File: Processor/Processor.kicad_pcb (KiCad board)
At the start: 2 copper layers, 100 x 100 mm, 43 parts, among them J1 Buss, J2 L2|L3, U1 MC6800, U10 74LS573, U11 74LS573, U2 74LS74, U3 74LS00, U4 74LS245, U5 74LS573, U6 74LS138, U7 GAL20V8, U8 74LS04, U9 74LS573, Y1 2.0MHz

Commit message: churn
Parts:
- added J3: L3, Connector_PinHeader_2.54mm:PinHeader_1x10_P2.54mm_Horizontal, F.Cu at (32.6, 35.2)
- J2: value L2|L3 -> L2; footprint Connector_PinSocket_2.54mm:PinSocket_2x08_P2.54mm_Horizontal -> Connector_PinHeader_2.54mm:PinHeader_1x10_P2.54mm_Horizontal
- moved C11 35.4 mm to (28.8, 42.7)
- moved U11 35.4 mm to (32.6, 47.8)
- moved RN3 20.3 mm to (96.1, 107.5), turned to 180 degrees
- moved J2 16.7 mm to (66.9, 35.2), turned to 90 degrees
- moved C9 3.85 mm to (93.6, 55.5)
- moved U9 3.85 mm to (97.2, 60.6)
- moved C10 3.81 mm to (93.6, 42.8)
- moved C3 3.81 mm to (28.8, 80.9)
- moved C8 3.81 mm to (28.8, 55.5)
- moved RN2 3.81 mm to (55.5, 107.5)
- moved U10 3.81 mm to (97.4, 47.9)
- moved U2 3.81 mm to (32.6, 73.3)
- moved U8 3.81 mm to (32.6, 60.6)
- moved U3 3.81 mm to (32.6, 86.0)
- moved C2 3.77 mm to (28.8, 68.2)
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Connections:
- J2 pad 1: Net-(J2-Pin_1) -> +5V
- J2 pad 10: Net-(J2-Pin_10) -> GND
- RN3 pad 2: A15 -> A8
- RN3 pad 3: A14 -> A9
- RN3 pad 4: A13 -> A10
- RN3 pad 5: A12 -> A11
- RN3 pad 6: A11 -> A12
- RN3 pad 7: A10 -> A13
- RN3 pad 8: A9 -> A14
- RN3 pad 9: A8 -> A15
- U11 pad 12: Net-(J2-Pin_16) -> Net-(J3-Pin_9)
- U11 pad 13: Net-(J2-Pin_14) -> Net-(J3-Pin_8)
- U11 pad 14: Net-(J2-Pin_12) -> Net-(J3-Pin_7)
- U11 pad 15: Net-(J2-Pin_10) -> Net-(J3-Pin_6)
- U11 pad 16: Net-(J2-Pin_8) -> Net-(J3-Pin_5)
- U11 pad 17: Net-(J2-Pin_6) -> Net-(J3-Pin_4)
- U11 pad 18: Net-(J2-Pin_4) -> Net-(J3-Pin_3)
- U11 pad 19: Net-(J2-Pin_2) -> Net-(J3-Pin_2)
- U5 pad 12: Net-(J2-Pin_15) -> Net-(J2-Pin_9)
- U5 pad 13: Net-(J2-Pin_13) -> Net-(J2-Pin_8)
- U5 pad 14: Net-(J2-Pin_11) -> Net-(J2-Pin_7)
- U5 pad 15: Net-(J2-Pin_9) -> Net-(J2-Pin_6)
- U5 pad 16: Net-(J2-Pin_7) -> Net-(J2-Pin_5)
- U5 pad 17: Net-(J2-Pin_5) -> Net-(J2-Pin_4)
- U5 pad 19: Net-(J2-Pin_1) -> Net-(J2-Pin_2)

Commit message: a bunch of stuff
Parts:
- removed C10, C11, C5, C9: 100n, Capacitor_THT:C_Disc_D3.0mm_W1.6mm_P2.50mm
- removed D1: S0, LED_THT:LED_Rectangular_W5.0mm_H2.0mm
- removed D2: S1, LED_THT:LED_Rectangular_W5.0mm_H2.0mm
- removed D3: S2, LED_THT:LED_Rectangular_W5.0mm_H2.0mm
- removed D4: S3, LED_THT:LED_Rectangular_W5.0mm_H2.0mm
- removed D5: S4, LED_THT:LED_Rectangular_W5.0mm_H2.0mm
- removed D6: S5, LED_THT:LED_Rectangular_W5.0mm_H2.0mm
- removed D7: S6, LED_THT:LED_Rectangular_W5.0mm_H2.0mm
- removed D8: S7, LED_THT:LED_Rectangular_W5.0mm_H2.0mm
- removed J2: L2, Connector_PinHeader_2.54mm:PinHeader_1x10_P2.54mm_Horizontal
- removed J3: L3, Connector_PinHeader_2.54mm:PinHeader_1x10_P2.54mm_Horizontal
- removed RN5: 220Ω, Resistor_THT:R_Array_SIP9
- removed U10, U11, U5, U9: 74LS573, Package_DIP:DIP-20_W7.62mm
- removed U6: 74LS138, Package_DIP:DIP-16_W7.62mm
- added G1: Logo, 0-Footprints:Crank, F.Cu at (32.7, 114.0)
- U7: value GAL20V8 -> GAL22V10
- moved C2 85.3 mm to (113.3, 79.4), turned to 180 degrees
- moved U2 76.2 mm to (108.3, 82.4), turned to 0 degrees
- moved C8 72.1 mm to (96.8, 79.4), turned to 180 degrees
- moved U8 63.1 mm to (91.8, 82.4), turned to 0 degrees
- moved Y1 57.2 mm to (113.9, 63.6), turned to 180 degrees
- moved C3 51.5 mm to (80.3, 79.4), turned to 180 degrees
- moved U3 42.8 mm to (75.3, 82.4), turned to 0 degrees
- moved R6 35.2 mm to (53.4, 61.6)
- moved C1 35.2 mm to (68.7, 56.5)
- moved R7 35.2 mm to (58.5, 61.6)
- moved R8 35.2 mm to (63.6, 61.6)
- moved U1 35.2 mm to (50.9, 54.0)
- moved U7 33.2 mm to (60.0, 69.7), turned to 0 degrees
- moved C7 30.9 mm to (65.1, 66.7), turned to 180 degrees
- moved C4 29.5 mm to (45.3, 71.7), turned to 180 degrees
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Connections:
- J1 pad 10: BANK_0 -> unconnected-(J1-Pad10)
- J1 pad 12: BANK_1 -> unconnected-(J1-Pad12)
- J1 pad 14: BANK_2 -> unconnected-(J1-Pad14)
- J1 pad 16: BANK_3 -> unconnected-(J1-Pad16)
- J1 pad 18: BANK_4 -> unconnected-(J1-Pad18)
- J1 pad 20: BANK_5 -> unconnected-(J1-Pad20)
- J1 pad 22: BANK_6 -> unconnected-(J1-Pad22)
- J1 pad 24: BANK_7 -> unconnected-(J1-Pad24)
- J1 pad 44: Φ2 -> unconnected-(J1-Pad44)
- J1 pad B3: unconnected-(J1-PadB3) -> Φ2
- U3 pad 10: Net-(U6-O1) -> GND
- U3 pad 11: LOAD_0 -> unconnected-(U3-Pad11)
- U3 pad 12: Net-(U6-O0) -> GND
- U3 pad 13: Net-(U6-O0) -> GND
- U3 pad 8: LOAD_1 -> unconnected-(U3-Pad8)
- U3 pad 9: Net-(U6-O1) -> GND
- U7 pad 10: A12 -> A8
- U7 pad 11: A11 -> GND
- U7 pad 13: A10 -> GND
- U7 pad 14: A9 -> GND
- U7 pad 17: ~{LATCH_SEL} -> GND
- U7 pad 18: BUS_OK -> GND
- U7 pad 19: ~{IO_SEL} -> BUS_OK
- U7 pad 20: ~{BANK_SEL} -> ~{IO_SEL}
- U7 pad 21: ~{ROM_SEL} -> ~{BANK_SEL}
- U7 pad 22: ~{RAM_SEL} -> ~{ROM_SEL}
- U7 pad 23: A8 -> ~{RAM_SEL}
- U7 pad 3: GND -> A15
- U7 pad 4: GND -> A14
- U7 pad 5: GND -> A13
- U7 pad 6: GND -> A12
- U7 pad 7: A15 -> A11
- U7 pad 8: A14 -> A10
- U7 pad 9: A13 -> A9
- U8 pad 10: LOAD_2 -> unconnected-(U8-Pad10)
- U8 pad 11: Net-(U6-O2) -> GND
- U8 pad 12: LOAD_3 -> unconnected-(U8-Pad12)
- U8 pad 13: Net-(U6-O3) -> GND

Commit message: ordered v01 of the cpu
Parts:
- removed C6, C7, C8: 100n, Capacitor_THT:C_Disc_D3.0mm_W1.6mm_P2.50mm
- removed the R6 at (53.4, 61.6)
- removed U3: 74LS00, Package_DIP:DIP-14_W7.62mm
- removed U8: 74LS04, Package_DIP:DIP-14_W7.62mm
- added C5: 100n, 0-Footprints:C_Disc_D5.0mm_W2.5mm_P5.00mm, F.Cu at (66.1, 55.5)
- added G2: Crankery, 0-Footprints:crankery_small, F.Cu at (112.7, 110.8)
- added G3: Motorola, 0-Footprints:Motorola, B.Cu at (69.3, 31.0)
- added G4: Crank, 0-Footprints:Crank, B.Cu at (103.4, 31.1)
- added R1: 10K, 0-Footprints:R_Axial_DIN0204_L3.6mm_D1.6mm_P7.62mm_Horizontal, F.Cu at (42.0, 66.9)
- added R2: 10K, 0-Footprints:R_Axial_DIN0204_L3.6mm_D1.6mm_P7.62mm_Horizontal, F.Cu at (92.8, 83.4)
- added R3: 10K, 0-Footprints:R_Axial_DIN0204_L3.6mm_D1.6mm_P7.62mm_Horizontal, F.Cu at (41.5, 107.5)
- added R4: 10K, 0-Footprints:R_Axial_DIN0204_L3.6mm_D1.6mm_P7.62mm_Horizontal, F.Cu at (58.5, 74.5)
- added R9: 10K, 0-Footprints:R_Axial_DIN0204_L3.6mm_D1.6mm_P7.62mm_Horizontal, F.Cu at (54.2, 107.5)
- added RN5: 4.7K, 0-Footprints:R_Array_SIP5, F.Cu at (62.3, 83.4)
- added RN6: 4.7K, 0-Footprints:R_Array_SIP5, F.Cu at (89.0, 93.6)
- added RN7: 4.7K, 0-Footprints:R_Array_SIP5, F.Cu at (66.1, 73.3)
- added RN8: 4.7K, 0-Footprints:R_Array_SIP5, F.Cu at (89.0, 58.0)
- C1: value 100n -> 100nF; footprint Capacitor_THT:C_Disc_D3.0mm_W1.6mm_P2.50mm -> 0-Footprints:C_Disc_D5.0mm_W2.5mm_P5.00mm
- C2, C3, C4: footprint Capacitor_THT:C_Disc_D3.0mm_W1.6mm_P2.50mm -> 0-Footprints:C_Disc_D5.0mm_W2.5mm_P5.00mm
- G1: value Logo -> Crank
- R5, R7, R8: footprint Resistor_THT:R_Axial_DIN0204_L3.6mm_D1.6mm_P5.08mm_Horizontal -> 0-Footprints:R_Axial_DIN0204_L3.6mm_D1.6mm_P7.62mm_Horizontal
- R6: renamed from R9; footprint Resistor_THT:R_Axial_DIN0204_L3.6mm_D1.6mm_P5.08mm_Horizontal -> 0-Footprints:R_Axial_DIN0204_L3.6mm_D1.6mm_P7.62mm_Horizontal
- RN1, RN2, RN3, RN4: footprint Resistor_THT:R_Array_SIP9 -> 0-Footprints:R_Array_SIP5
- U1: value MC6800 -> M6800; footprint Package_DIP:DIP-40_W15.24mm -> 0-Footprints:DIP-40_W15.24mm
- U2: value 74LS74 -> MC6875; footprint Package_DIP:DIP-14_W7.62mm -> 0-Footprints:DIP-16_W7.62mm
- U4: footprint Package_DIP:DIP-20_W7.62mm -> 0-Footprints:DIP-20_W7.62mm
- U7: footprint Package_DIP:DIP-24_W7.62mm -> 0-Footprints:DIP-24_W7.62mm
- Y1: value 2.0MHz -> 4.000MHz; footprint Oscillator:Oscillator_DIP-14 -> 0-Footprints:Oscillator_DIP-14
- moved G1 82.9 mm to (35.6, 31.2)
- moved R6 72.4 mm to (46.6, 107.5), turned to -90 degrees
- moved U2 65.2 mm to (54.7, 45.3)
- moved RN2 64.3 mm to (92.8, 68.2)
- moved Y1 64.3 mm to (49.6, 62.1), turned to 90 degrees
- moved U4 63.1 mm to (96.0, 45.3)
- moved RN4 55.6 mm to (106.8, 68.2), turned to 90 degrees
- moved RN1 48.6 mm to (110.6, 60.6), turned to 90 degrees
- moved R8 48.2 mm to (49.1, 107.5), turned to -90 degrees
- moved R7 46.0 mm to (58.0, 107.5), turned to -90 degrees
- moved RN3 43.8 mm to (62.3, 77.1), turned to 90 degrees
- moved R5 40.7 mm to (44.5, 66.9), turned to -90 degrees
- moved C1 38.6 mm to (106.8, 50.3), turned to 90 degrees
- moved U7 36.1 mm to (96.0, 73.3)
- moved C4 29.9 mm to (66.1, 50.3), turned to 90 degrees
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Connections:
- net 2.0MHz renamed Net-(U2-EXT_IN)
- C1 pad 1: +5V -> GND
- C1 pad 2: GND -> +5V
- C2 pad 1: +5V -> GND
- C2 pad 2: GND -> +5V
- C3 pad 1: +5V -> GND
- C3 pad 2: GND -> +5V
- C4 pad 1: +5V -> GND
- C4 pad 2: GND -> +5V
- J1 pad 36: unconnected-(J1-Pad36) -> MEM_CLK
- J1 pad 38: unconnected-(J1-Pad38) -> DMA_GRANT
- J1 pad 40: unconnected-(J1-Pad40) -> MEMRDY
- J1 pad 42: unconnected-(J1-Pad42) -> ~{DMA_REQ}
- J1 pad 44: unconnected-(J1-Pad44) -> ~{POR}
- J1 pad P1: (no net) -> +5V
- J1 pad P2: (no net) -> GND
- J1 pad P3: (no net) -> unconnected-(J1-+12V-PadP3)
- J1 pad P4: (no net) -> unconnected-(J1--12V-PadP4)
- R5 pad 2: R/~{W} -> MEMRDY
- RN1 pad 2: A0 -> D3
- RN1 pad 3: A1 -> D2
- RN1 pad 4: A2 -> D1
- RN1 pad 5: A3 -> D0
- RN3 pad 2: A8 -> A3
- RN3 pad 3: A9 -> A2
- RN3 pad 4: A10 -> A1
- RN3 pad 5: A11 -> A0
- RN4 pad 2: D0 -> D7
- RN4 pad 3: D1 -> D6
- RN4 pad 4: D2 -> D5
- RN4 pad 5: D3 -> D4
- U1 pad 36: ~{DBE} -> DBE
- U1 pad 37: Φ2 -> Net-(U1-Phi2)
- U2 pad 1: +5V -> GND
- U2 pad 10: GND -> ~{DMA_REQ}
- U2 pad 11: GND -> DMA_GRANT
- U2 pad 12: GND -> ~{POR}
- U2 pad 13: GND -> Net-(U1-Phi2)
- U2 pad 14: +5V -> ~{RESET}
- U2 pad 2: CLK_B -> unconnected-(U2-X2-Pad2)
- U2 pad 4: +5V -> unconnected-(U2-4x_fo-Pad4)
- U2 pad 5: CLK_A -> unconnected-(U2-2x_fo-Pad5)
- U2 pad 6: CLK_B -> MEMRDY
- U2 pad 7: GND -> Φ2
- U2 pad 8: unconnected-(U2B-~{Q}-Pad8) -> GND
- U2 pad 9: unconnected-(U2B-Q-Pad9) -> MEM_CLK
- U7 pad 10: A8 -> A9
- U7 pad 11: GND -> A8
- U7 pad 3: A15 -> VMA
- U7 pad 4: A14 -> A15
- U7 pad 5: A13 -> A14
- U7 pad 6: A12 -> A13
- U7 pad 7: A11 -> A12
- U7 pad 8: A10 -> A11
- U7 pad 9: A9 -> A10
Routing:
- net +5V: track 0.00 -> 315.9 mm, vias 0 -> 11
- net VMA: track 0.00 -> 132.8 mm, vias 0 -> 3
- net ~{TSC}: track 0.00 -> 120.0 mm, vias 0 -> 3
- net MEMRDY: track 0.00 -> 118.3 mm, vias 0 -> 3
- net ~{RESET}: track 0.00 -> 118.0 mm, vias 0 -> 5
- net Φ2: track 0.00 -> 115.9 mm, vias 0 -> 3
- net ~{DMA_REQ}: track 0.00 -> 113.6 mm, vias 0 -> 3
- net ~{HALT}: track 0.00 -> 111.8 mm, vias 0 -> 4
- net BD3: track 0.00 -> 105.5 mm, vias 0 -> 2
- net A1: track 0.00 -> 105.0 mm, vias 0 -> 3
- net A0: track 0.00 -> 105.0 mm, vias 0 -> 1
- net DBE: track 0.00 -> 103.2 mm, vias 0 -> 3
- net BD4: track 0.00 -> 100.8 mm, vias 0 -> 2
- net BD5: track 0.00 -> 99.8 mm, vias 0 -> 2
- net BD6: track 0.00 -> 98.5 mm, vias 0 -> 2
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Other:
- board text added: "C68 CPU"
- board text added: "C68CPU.01"
- board text added: "Crankery - April 2026 - Dave Hamilton"
- board text added: "JLCJLCJLCJLC"
- board text added: "Motorola M6800"

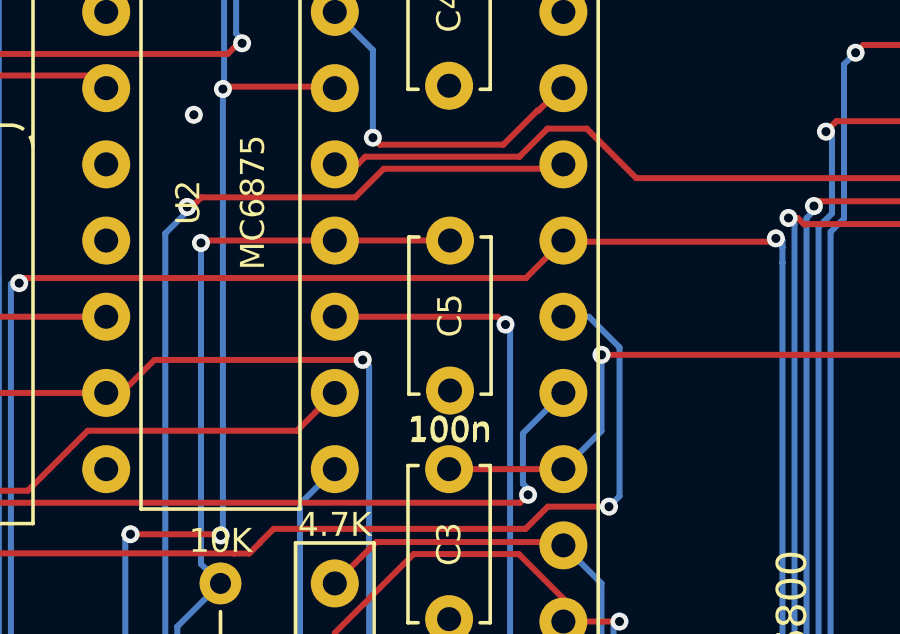
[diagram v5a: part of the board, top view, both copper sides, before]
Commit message: lots of fixes to stack handling on emu, fix the latches on the banked memory board, tons of little bug fixes
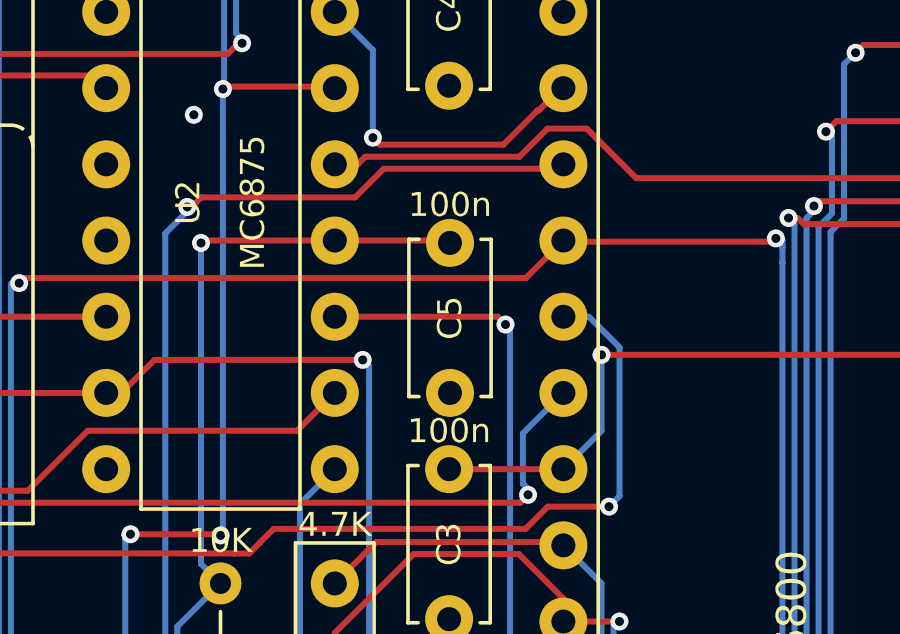
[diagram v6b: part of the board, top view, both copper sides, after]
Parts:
- moved C5 5.08 mm to (66.1, 60.6), turned to 90 degrees
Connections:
- C5 pad 1: ~{POR} -> GND
- C5 pad 2: GND -> ~{POR}
